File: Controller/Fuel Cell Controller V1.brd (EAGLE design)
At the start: 100 x 80 mm, 4 parts

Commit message: update
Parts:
- added H2BOARD, H2BOARD1: ETHERNET, ETHERNET:A122645-ND
- added R1: 10k, adafruit:R0603
- added U$4: DS3231, DS3231:DS3231
- moved FRAME1 62.5 mm to (-14.0, 57.1)
- moved U$2 32.1 mm to (29.2, 11.4)
- moved U$1 19.1 mm to (52.1, 20.3)
- moved U$3 9.92 mm to (74.9, 40.6)
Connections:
- removed net N$1: U$2.P$1
- removed net N$5: U$3.RST
- removed net N$6: U$3.ALR
- removed net N$7: U$3.ADR
- new net 12V_AUX: H2BOARD.P$6
- new net 5V: H2BOARD.P$8, H2BOARD1.P$5
- new net CAPCURR: H2BOARD1.P$1, U$1.17/A3
- new net CAPVOLT: H2BOARD1.P$3, U$1.14/A0
- new net EXTRA_SIG: H2BOARD.P$2
- new net FCCURR: H2BOARD1.P$2, U$1.15/A1
- new net FCVOLT: H2BOARD1.P$4, U$1.16/A2
- new net FC_R: H2BOARD1.P$6
- new net H2_OK: H2BOARD.P$1, R1.2, U$1.2
- net +3.3V: now also U$4.P$1
- net GND: now also H2BOARD.P$13, H2BOARD.P$14, H2BOARD.P$5, H2BOARD1.P$13, H2BOARD1.P$14, H2BOARD1.P$7, H2BOARD1.P$8, R1.1, U$4.P$2
- net SCL: now also U$4.P$3
- net SDA: now also U$4.P$4
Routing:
- removed copper zone on layer 1, net GND
- removed copper zone on layer 16, net GND
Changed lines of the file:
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@@
 </autorouter>
 <elements>
-<element name="FRAME1" library="SparkFun-Aesthetics" package="DUMMY" value="FRAME-LETTERNO_PACKAGE" x="-41.91" y="1.27">
-<attribute name="DESIGNER" value="Reegan McAllister" x="-41.91" y="1.27" size="1.778" layer="27" display="off"/>
-<attribute name="VERSION" value="v01" x="-41.91" y="1.27" size="1.778" layer="27" display="off"/>
+<element name="FRAME1" library="SparkFun-Aesthetics" package="DUMMY" value="FRAME-LETTERNO_PACKAGE" x="-13.97" y="57.15">
+<attribute name="DESIGNER" value="Reegan McAllister" x="-13.97" y="57.15" size="1.778" layer="27" display="off"/>
+<attribute name="VERSION" value="v01" x="-13.97" y="57.15" size="1.778" layer="27" display="off"/>
 </element>
-<element name="U$1" library="Teensy_3_and_LC_Series_Boards_v1.1" package="TEENSY3-ALL_PINS" value="TEENSY_3.1_ALL_PINS" x="53.34" y="39.37"/>
-<element name="U$2" library="openlog" package="OPENLOG" value="OPENLOG" x="11.43" y="38.1" rot="R90"/>
-<element name="U$3" library="SHT31Breakout" package="SHT31-BREAKOUT" value="SHT31-BREAKOUT" x="67.31" y="34.29"/>
+<element name="U$1" library="Teensy_3_and_LC_Series_Boards_v1.1" package="TEENSY3-ALL_PINS" value="TEENSY_3.1_ALL_PINS" x="52.07" y="20.32"/>
+<element name="U$2" library="openlog" package="OPENLOG" value="OPENLOG" x="29.21" y="11.43" rot="R90"/>
+<element name="U$3" library="SHT31Breakout" package="SHT31-BREAKOUT" value="SHT31-BREAKOUT" x="74.93" y="40.64"/>
+<element name="U$4" library="DS3231" package="DS3231" value="DS3231" x="73.66" y="57.15"/>
+<element name="H2BOARD" library="ETHERNET" package="A122645-ND" value="ETHERNET" x="57.15" y="63.5"/>
+<element name="R1" library="adafruit" package="R0603" value="10k" x="76.2" y="21.59"/>
+<element name="H2BOARD1" library="ETHERNET" package="A122645-ND" value="ETHERNET" x="78.74" y="6.35"/>
 </elements>
 <signals>
@@
 <contactref element="U$1" pad="18/A4"/>
 <contactref element="U$3" pad="SDA"/>
-<wire x1="60.96" y1="35.56" x2="76.2" y2="36.83" width="0" layer="19" extent="1-1"/>
+<contactref element="U$4" pad="P$4"/>
+<wire x1="83.82" y1="43.18" x2="83.82" y2="59.69" width="0" layer="19" extent="1-1"/>
+<wire x1="59.69" y1="16.51" x2="83.82" y2="43.18" width="0" layer="19" extent="1-1"/>
 </signal>
 <signal name="SCL">
 <contactref element="U$1" pad="19/A5"/>
 <contactref element="U$3" pad="SCL"/>
-<wire x1="60.96" y1="38.1" x2="73.66" y2="36.83" width="0" layer="19" extent="1-1"/>
+<contactref element="U$4" pad="P$3"/>
+<wire x1="81.28" y1="43.18" x2="81.28" y2="59.69" width="0" layer="19" extent="1-1"/>
+<wire x1="59.69" y1="19.05" x2="81.28" y2="43.18" width="0" layer="19" extent="1-1"/>
 </signal>
 <signal name="+5V">
@@
 <contactref element="U$3" pad="VIN"/>
 <contactref element="U$2" pad="P$4"/>
-<wire x1="68.58" y1="36.83" x2="60.96" y2="50.8" width="0" layer="19" extent="1-1"/>
-<wire x1="50.8" y1="22.86" x2="68.58" y2="36.83" width="0" layer="19" extent="1-1"/>
-<wire x1="19.685" y1="39.37" x2="50.8" y2="22.86" width="0" layer="19" extent="1-1"/>
+<contactref element="U$4" pad="P$1"/>
+<wire x1="76.2" y1="43.18" x2="76.2" y2="59.69" width="0" layer="19" extent="1-1"/>
+<wire x1="59.69" y1="31.75" x2="76.2" y2="43.18" width="0" layer="19" extent="1-1"/>
+<wire x1="37.465" y1="12.7" x2="59.69" y2="31.75" width="0" layer="19" extent="1-1"/>
+<wire x1="49.53" y1="3.81" x2="37.465" y2="12.7" width="0" layer="19" extent="1-1"/>
 </signal>
 <signal name="GND">
@@
 <contactref element="U$2" pad="P$6"/>
 <contactref element="U$2" pad="P$5"/>
-<polygon width="0.4064" layer="1">
-<vertex x="-25.4" y="130.81"/>
-<vertex x="255.27" y="130.81"/>
-<vertex x="255.27" y="-13.97"/>
-<vertex x="-24.13" y="-13.97"/>
-</polygon>
-<polygon width="0.4064" layer="16">
-<vertex x="-25.4" y="130.81"/>
-<vertex x="255.27" y="130.81"/>
-<vertex x="255.27" y="-12.7"/>
-<vertex x="-24.13" y="-12.7"/>
-</polygon>
+<contactref element="U$4" pad="P$2"/>
+<contactref element="H2BOARD" pad="P$5"/>
+<contactref element="H2BOARD" pad="P$13"/>
+<contactref element="H2BOARD" pad="P$14"/>
+<contactref element="R1" pad="1"/>
+<contactref element="H2BOARD1" pad="P$7"/>
+<contactref element="H2BOARD1" pad="P$8"/>
+<contactref element="H2BOARD1" pad="P$13"/>
+<contactref element="H2BOARD1" pad="P$14"/>
+<wire x1="65.28" y1="66.93" x2="78.74" y2="59.69" width="0" layer="19" extent="1-1"/>
+<wire x1="56.65" y1="66.04" x2="65.28" y2="66.93" width="0" layer="19" extent="1-1"/>
+<wire x1="49.02" y1="66.93" x2="56.65" y2="66.04" width="0" layer="19" extent="1-1"/>
+<wire x1="78.74" y1="43.18" x2="78.74" y2="59.69" width="0" layer="19" extent="1-1"/>
+<wire x1="75.35" y1="21.59" x2="78.74" y2="43.18" width="0" layer="19" extent="1-1"/>
+<wire x1="75.18" y1="10.67" x2="75.35" y2="21.59" width="0" layer="19" extent="1-1"/>
+<wire x1="76.2" y1="8.89" x2="75.18" y2="10.67" width="0" layer="19" extent="1-1"/>
+<wire x1="70.61" y1="9.78" x2="75.18" y2="10.67" width="0" layer="19" extent="1-1"/>
+<wire x1="86.87" y1="9.78" x2="76.2" y2="8.89" width="0" layer="19" extent="1-1"/>
+<wire x1="52.07" y1="3.81" x2="70.61" y2="9.78" width="0" layer="19" extent="1-1"/>
+<wire x1="37.465" y1="15.24" x2="52.07" y2="3.81" width="0" layer="19" extent="1-1"/>
+<wire x1="37.465" y1="17.78" x2="37.465" y2="15.24" width="0" layer="19" extent="1-1"/>
+<wire x1="44.45" y1="36.83" x2="37.465" y2="17.78" width="0" layer="19" extent="1-1"/>
 </signal>
 <signal name="AREF">
@@
 <contactref element="U$1" pad="7"/>
 <contactref element="U$2" pad="P$3"/>
-<wire x1="19.685" y1="36.83" x2="45.72" y2="35.56" width="0" layer="19" extent="1-1"/>
+<wire x1="37.465" y1="10.16" x2="44.45" y2="16.51" width="0" layer="19" extent="1-1"/>
 </signal>
 <signal name="TX3">
 <contactref element="U$1" pad="8"/>
 <contactref element="U$2" pad="P$2"/>
-<wire x1="19.685" y1="34.29" x2="45.72" y2="33.02" width="0" layer="19" extent="1-1"/>
+<wire x1="37.465" y1="7.62" x2="44.45" y2="13.97" width="0" layer="19" extent="1-1"/>
 </signal>
-<signal name="N$5">
-<contactref element="U$3" pad="RST"/>
+<signal name="H2_OK">
+<contactref element="H2BOARD" pad="P$1"/>
+<contactref element="U$1" pad="2"/>
+<contactref element="R1" pad="2"/>
+<wire x1="44.45" y1="29.21" x2="60.73" y2="66.04" width="0" layer="19" extent="1-1"/>
+<wire x1="77.05" y1="21.59" x2="44.45" y2="29.21" width="0" layer="19" extent="1-1"/>
 </signal>
-<signal name="N$6">
-<contactref element="U$3" pad="ALR"/>
+<signal name="EXTRA_SIG">
+<contactref element="H2BOARD" pad="P$2"/>
 </signal>
-<signal name="N$7">
-<contactref element="U$3" pad="ADR"/>
+<signal name="5V">
+<contactref element="H2BOARD" pad="P$8"/>
+<contactref element="H2BOARD1" pad="P$5"/>
+<wire x1="78.24" y1="8.89" x2="53.59" y2="67.82" width="0" layer="19" extent="1-1"/>
 </signal>
-<signal name="N$1">
-<contactref element="U$2" pad="P$1"/>
+<signal name="12V_AUX">
+<contactref element="H2BOARD" pad="P$6"/>
+</signal>
+<signal name="CAPCURR">
+<contactref element="H2BOARD1" pad="P$1"/>
+<contactref element="U$1" pad="17/A3"/>
+<wire x1="59.69" y1="13.97" x2="82.32" y2="8.89" width="0" layer="19" extent="1-1"/>
+</signal>
+<signal name="FCCURR">
+<contactref element="H2BOARD1" pad="P$2"/>
+<contactref element="U$1" pad="15/A1"/>
+<wire x1="59.69" y1="8.89" x2="81.3" y2="10.67" width="0" layer="19" extent="1-1"/>
+</signal>
+<signal name="CAPVOLT">
+<contactref element="H2BOARD1" pad="P$3"/>
+<contactref element="U$1" pad="14/A0"/>
+<wire x1="59.69" y1="6.35" x2="80.28" y2="8.89" width="0" layer="19" extent="1-1"/>
+</signal>
+<signal name="FCVOLT">
+<contactref element="H2BOARD1" pad="P$4"/>
+<contactref element="U$1" pad="16/A2"/>
+<wire x1="59.69" y1="11.43" x2="79.26" y2="10.67" width="0" layer="19" extent="1-1"/>
+</signal>
+<signal name="FC_R">
+<contactref element="H2BOARD1" pad="P$6"/>
 </signal>
 </signals>

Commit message: update
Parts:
- removed H2BOARD1: ETHERNET, ETHERNET:A122645-ND
- added CVM, POWERBOARD, PRESSURE, RELAY1, RELAY2: ETHERNET, ETHERNET:A122645-ND
- added FRAME2: FRAME-LETTERNO_PACKAGE, SparkFun-Aesthetics:DUMMY
- added U$5: RS232-TO-CAN-CONVERTER, rs232-to-can:RS232-TO-CAN-CONVERTER
- moved H2BOARD 12.7 mm to (57.1, 76.2), turned to 180 degrees
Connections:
- removed net 12V_AUX: H2BOARD.P$6
- removed net FC_R: H2BOARD1.P$6
- removed net MISO: U$1.12
- removed net MOSI: U$1.11
- removed net SCK: U$1.13
- new net AUX12: H2BOARD.P$6, POWERBOARD.P$3, RELAY1.P$5
- new net CAP_R: RELAY1.P$3, U$1.11
- new net CHARGE_R: RELAY1.P$4, U$1.12
- new net EXTRA_V: U$1.10
- new net FC12: POWERBOARD.P$1, POWERBOARD.P$2, PRESSURE.P$1, RELAY1.P$6
- new net FCC_R: POWERBOARD.P$8, RELAY2.P$6, U$1.20/A6
- new net FCPRES: PRESSURE.P$3, U$1.23/A9
- new net MOTOR_R: RELAY1.P$2, U$1.22/A8
- new net N$1: CVM.P$1
- new net N$2: CVM.P$2
- new net N$3: CVM.P$3
- new net N$4: CVM.P$4
- new net N$5: CVM.P$5
- new net N$6: CVM.P$6
- new net N$7: CVM.P$7
- new net N$8: CVM.P$8
- new net PURGE_V: U$1.9
- new net START_R: RELAY1.P$1, U$1.21/A7
- new net SUPPLY_V: U$1.6
- net 5V: now also POWERBOARD.P$4, RELAY2.P$5, U$5.5V, U$5.VCC; no longer H2BOARD1.P$5
- net CAPCURR: now also RELAY2.P$1; no longer H2BOARD1.P$1
- net CAPVOLT: now also RELAY2.P$3; no longer H2BOARD1.P$3
- net FCCURR: now also RELAY2.P$2; no longer H2BOARD1.P$2
- net FCVOLT: now also RELAY2.P$4; no longer H2BOARD1.P$4
- net GND: now also CVM.P$13, CVM.P$14, POWERBOARD.P$13, POWERBOARD.P$14, POWERBOARD.P$5, POWERBOARD.P$6, POWERBOARD.P$7, PRESSURE.P$2, RELAY1.P$13, RELAY1.P$14, RELAY1.P$7, RELAY1.P$8, RELAY2.P$13, RELAY2.P$14, RELAY2.P$7, RELAY2.P$8, U$5.GND, U$5.GND_; no longer H2BOARD1.P$13, H2BOARD1.P$14, H2BOARD1.P$7, H2BOARD1.P$8
- net RX1: now also U$5.TX0
- net TX1: now also U$5.RXI

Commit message: update
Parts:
- removed POWERBOARD: ETHERNET, ETHERNET:A122645-ND
- added AUXPOWER, FCPOWER: 5555140-6, 5555140-6 RJ11:1734723-1_RJ11
- added U$7: FAN-CONTROLLER, fan controller:FAN-CONTROLLER
- added U$8: MOSFETBOARD, mosfet board:MOSFET-BOARD
- added VALVES: ETHERNET, ETHERNET:A122645-ND
- moved U$5 260.7 mm to (106.7, 105.4), turned to 270 degrees
- moved R1 71.2 mm to (10.2, 48.3)
- moved U$3 53.4 mm to (21.6, 38.1), turned to 270 degrees
- moved PRESSURE 44.5 mm to (57.1, 3.81)
- moved U$1 42.3 mm to (24.1, 52.1), turned to 90 degrees
- moved CVM 20.4 mm to (5.08, 30.5)
- moved U$2 19.4 mm to (10.2, 7.62), turned to 180 degrees
- moved H2BOARD 18.8 mm to (66.0, 92.7)
- moved RELAY1 17.7 mm to (39.4, 92.7)
- moved RELAY2 16.9 mm to (15.2, 92.7)
- moved U$4 16.6 mm to (74.9, 73.7), turned to 180 degrees
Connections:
- removed net +5V: U$1.VIN
- new net AUX5: AUXPOWER.3, AUXPOWER.4, H2BOARD.P$8, U$5.5V, U$5.VCC
- new net EXTRA_V_G: U$8.OUT3, VALVES.P$6
- new net FC5: FCPOWER.3, FCPOWER.4, U$1.VIN, U$2.P$4, U$7.5, U$7.5_2, U$8.VDD
- new net N$16: PRESSURE.P$4
- new net N$17: PRESSURE.P$5
- new net N$18: PRESSURE.P$6
- new net N$19: PRESSURE.P$7
- new net N$20: PRESSURE.P$8
- new net N$21: PRESSURE.P$13
- new net N$22: PRESSURE.P$14
- new net PURGE_V_G: U$8.OUT2, VALVES.P$4
- new net SUPPLY_V_G: U$8.OUT1, VALVES.P$2
- net +3.3V: no longer U$2.P$4
- net 5V: no longer H2BOARD.P$8, POWERBOARD.P$4, U$5.5V, U$5.VCC
- net AUX12: now also AUXPOWER.1, AUXPOWER.2, VALVES.P$1; no longer POWERBOARD.P$3
- net EXTRA_V: now also U$8.IN3
- net FC12: now also FCPOWER.1, FCPOWER.2, U$7.12, U$7.12_2, U$7.12_3, VALVES.P$3, VALVES.P$5; no longer POWERBOARD.P$1, POWERBOARD.P$2
- net FCC_R: no longer POWERBOARD.P$8
- net GND: now also AUXPOWER.5, AUXPOWER.6, AUXPOWER.SH1, AUXPOWER.SH2, FCPOWER.5, FCPOWER.6, FCPOWER.SH1, FCPOWER.SH2, U$7.GND, U$7.GND2, U$7.GND3, U$8.GND, U$8.GND1, U$8.GND2, U$8.VSS, VALVES.P$13, VALVES.P$14; no longer POWERBOARD.P$13, POWERBOARD.P$14, POWERBOARD.P$5, POWERBOARD.P$6, POWERBOARD.P$7
- net H2_OK: now also U$8.ESTOP
- net PURGE_V: now also U$8.IN2
- net SCL: now also U$7.SCL
- net SDA: now also U$7.SDA
- net SUPPLY_V: now also U$8.IN1
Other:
- board size 100 x 80 mm -> 160 x 100 mm

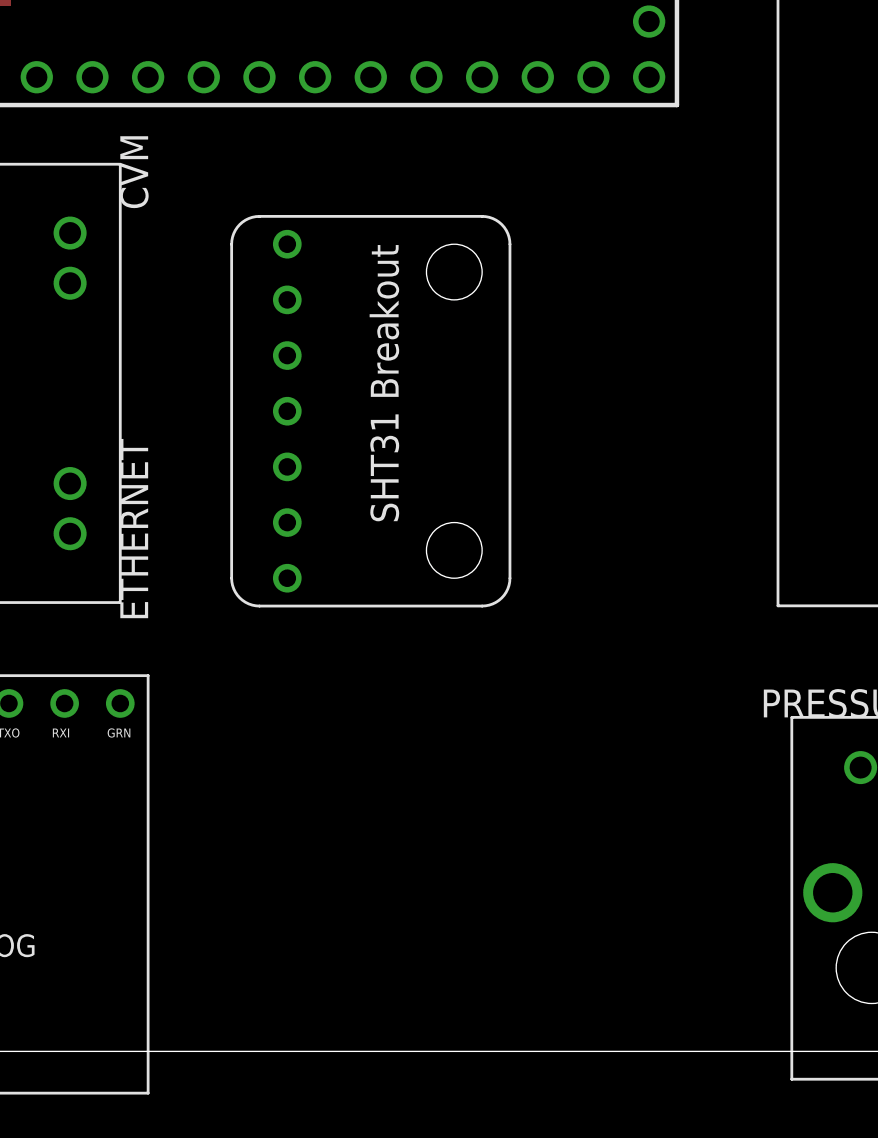
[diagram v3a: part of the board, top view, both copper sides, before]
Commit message: added rs 232 converter
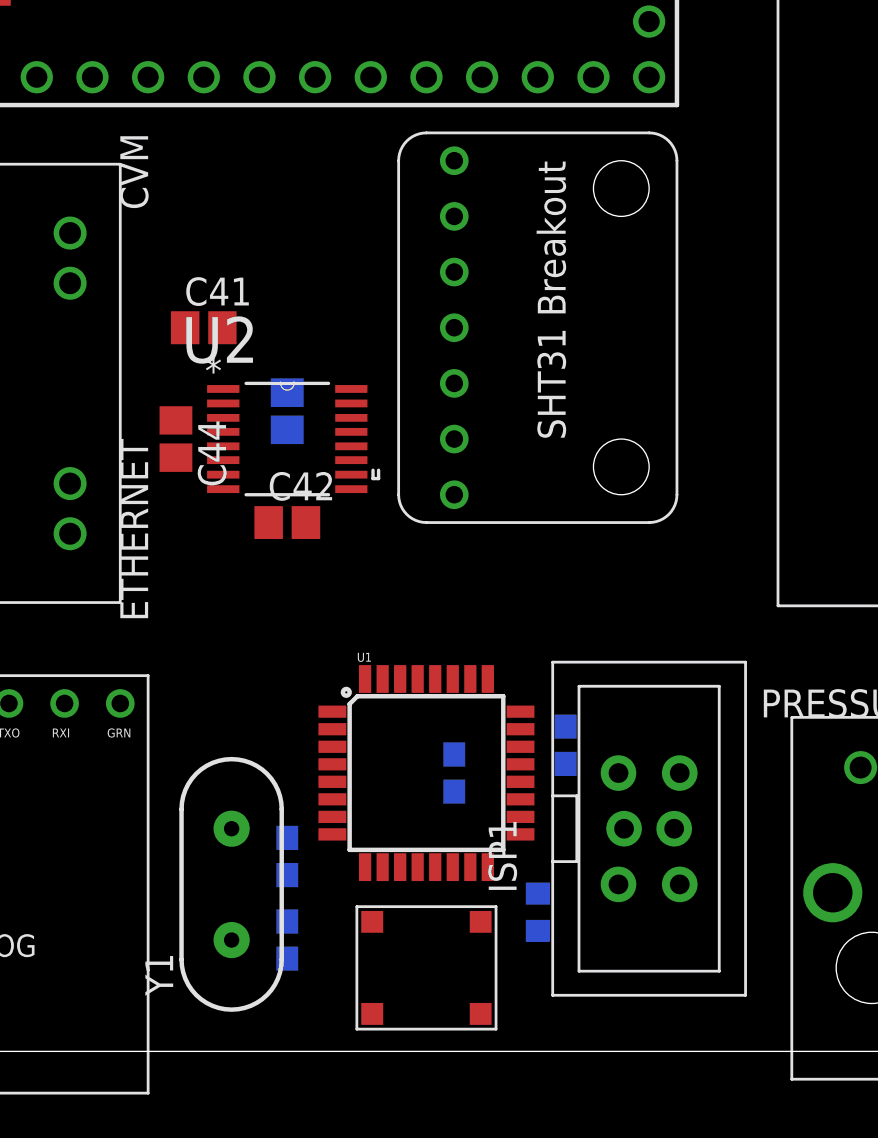
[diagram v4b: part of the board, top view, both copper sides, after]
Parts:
- added C1, C2, C3, C4: (no value), adafruit:C0603
- added C41, C42, C44: 0.33uF/12V, E-P-008-R1.2:C0805
- added C43: 0.047uF/12V, E-P-008-R1.2:C0805
- added FRAME3, FRAME4: FRAME-LETTERNO_PACKAGE, SparkFun-Aesthetics:DUMMY
- added ISP1: AVRISP-BOX, adafruit:AVRISP-BOX
- added R2: (no value), adafruit:R0603
- added U$6: EG4621CT-ND, EG4621CT-ND:EG4621CT-ND
- added U1: ATMEGA328P_TQFP, SparkFun-DigitalIC:TQFP32-08
- added U2: MAX3221CPWR, Texas Instruments_By_element14_Batch_1:SOP65P640X120-16N
- added Y1: (no value), SparkFun-FreqCtrl:HC49US
- moved U$3 8.52 mm to (29.2, 41.9)
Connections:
- net N$5 renamed CVMSIG1
- net N$6 renamed CVMSIG2
- net N$7 renamed CVMSIG3
- net N$8 renamed CVMSIG4
- removed net N$1: CVM.P$1
- removed net N$2: CVM.P$2
- removed net N$3: CVM.P$3
- new net ATMEG_RESET: ISP1.5, R2.1, U$6.P$3, U$6.P$4, U1.29
- new net CVMRX: U1.30, U2.9
- new net CVMTX: U1.31, U2.11
- new net MISO: ISP1.1, U1.16
- new net MOSI: ISP1.4, U1.15
- new net N$5: C2.1, U1.8, Y1.1
- new net N$73: C41.1, U2.3
- new net N$74: C43.1, U2.2
- new net N$75: C43.2, U2.4
- new net N$76: C44.1, U2.5
- new net N$77: C44.2, U2.6
- new net N$78: C42.1, U2.7
- new net RX12: CVM.P$3, U2.8
- new net SCK: ISP1.3, U1.17
- new net SER_INVALID: U2.10
- new net TX12: CVM.P$2, U2.13
- new net V+: U2.16
- new net VCC: ISP1.2
- net +3.3V: now also C3.1, C4.1, R2.2, U1.18, U1.20, U1.4, U1.6, U2.15
- net FC5: now also CVM.P$1
- net GND: now also C1.2, C2.2, C3.2, C4.2, C41.2, C42.2, CVM.P$4, ISP1.6, U$6.P$1, U$6.P$2, U1.21, U1.3, U1.5, U2.1, U2.12, U2.14
- net N$4: now also C1.1, U1.7, Y1.2; no longer CVM.P$4
- net SCL: now also U1.28
- net SDA: now also U1.27
